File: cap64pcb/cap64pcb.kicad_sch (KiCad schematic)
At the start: 1 part

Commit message: first draft sch
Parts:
- added C1, C3: 10uF, Capacitor_SMD:C_0805_2012Metric, symbol Device:C_Small
- added C2: 1uF, Capacitor_SMD:C_0805_2012Metric, symbol Device:C_Small
- added C4, C5: 0.1uF, Capacitor_SMD:C_0805_2012Metric, symbol Device:C_Small
- added J1: SM05B_SURS_TF, Connector_JST:JST_SUR_SM05B-SURS-TF_1x05-1MP_P0.80mm_Horizontal, symbol Connector_Generic:Conn_01x05
- added JP1, JP2, JP3: SolderJumper_2_Open, Jumper:SolderJumper-2_P1.3mm_Open_RoundedPad1.0x1.5mm, symbol Jumper:SolderJumper_2_Open
- added JP4: SolderJumper_2_Bridged, Jumper:SolderJumper-2_P1.3mm_Bridged_RoundedPad1.0x1.5mm, symbol Jumper:SolderJumper_2_Bridged
- added Q1, Q2: BSS138, Package_TO_SOT_SMD:SOT-23, symbol Transistor_FET:BSS138
- added R1: 75kΩ, Resistor_SMD:R_0805_2012Metric, symbol Device:R_Small
- added TP1, TP10, TP11, TP12, TP2, TP3, TP4, TP5, TP6, TP7, TP8, TP9: TestPoint_Alt, symbol Connector:TestPoint_Alt
- added U2: SPX3819M5-L-3-3, Package_TO_SOT_SMD:SOT-23-5, symbol Regulator_Linear:SPX3819M5-L-3-3
- gave numbers to parts that had none: 1
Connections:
- net INT: now reaches U1.1 (~{IRQ})
- net INT: now also J1.4 (Pin_4)
- net at U1.10 (ELE2): now also TP3.1
- net at U1.11 (ELE3): now also TP4.1
- net at U1.12 (LED0/ELE4): now also TP5.1
- net at U1.13 (LED1/ELE5): now also TP6.1
- net at U1.14 (LED2/ELE6): now also TP7.1
- net at U1.15 (LED3/ELE7): now also TP8.1
- net at U1.16 (LED4/ELE8): now also TP9.1
- net at U1.17 (LED5/ELE9): now also TP10.1
- net at U1.18 (LED6/ELE10): now also TP11.1
- net at U1.19 (LED7/ELE11): now also TP12.1
- net SCL: now reaches U1.2 (SCL)
- net SCL: now also JP3.1 (A), Q2.2 (S)
- net +3V3: now reaches U1.20 (VDD)
- net +3V3: now also C3.1, C4.1, JP1.1 (A), Q1.1 (G), Q2.1 (G), U2.5 (OUT)
- net SDA: now reaches U1.3 (SDA)
- net SDA: now also JP2.1 (A), Q1.2 (S)
- net at U1.4 (ADDR): now also JP1.2 (B), JP2.2 (B), JP3.2 (B), JP4.2 (B)
- net at U1.5 (VREG): now also C5.1
- net GND: now reaches U1.6 (VSS)
- net GND: now also C1.2, C2.2, C3.2, C4.2, C5.2, J1.5 (Pin_5), JP4.1 (A), R1.2, U2.2 (GND)
- net at U1.7 (REXT): now also R1.1
- net at U1.8 (ELE0): now also TP1.1
- net at U1.9 (ELE1): now also TP2.1
- new net: C2.1, U2.4 (BP)
- new net: J1.2 (Pin_2), Q1.3 (D)
- new net: J1.3 (Pin_3), Q2.3 (D)
- new net VCC: C1.1, J1.1 (Pin_1), U2.1 (IN), U2.3 (EN)
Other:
- company: (none) -> beadybiddle
- title: (none) -> cap64
- moved on the sheet: U1

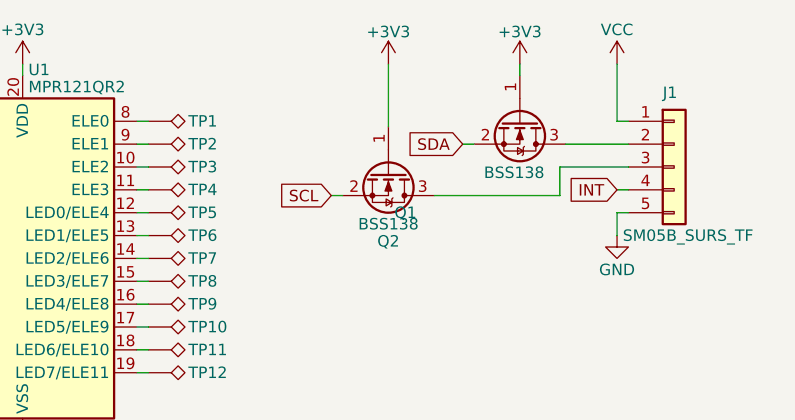
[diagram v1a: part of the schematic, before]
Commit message: pullup i2c 3v3 side lines
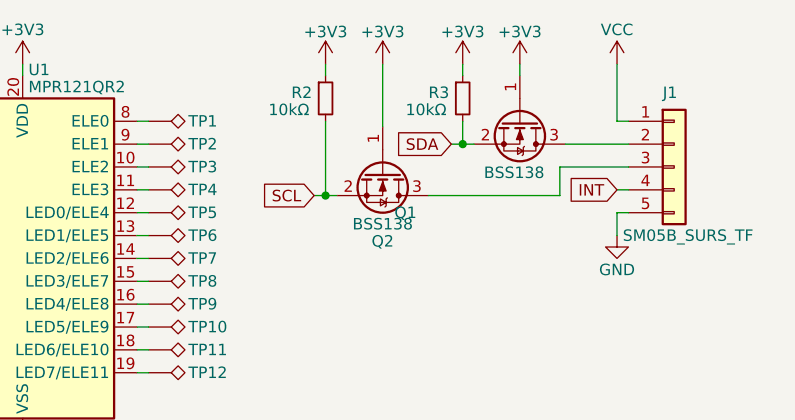
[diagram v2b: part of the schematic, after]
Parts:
- added R2, R3: 10kΩ, Resistor_SMD:R_0805_2012Metric, symbol Device:R_Small
- JP1: value SolderJumper_2_Open -> 3V3
- JP2: value SolderJumper_2_Open -> SDA
- JP3: value SolderJumper_2_Open -> SCL
- JP4: value SolderJumper_2_Bridged -> GND
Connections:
- net +3V3: now also R2.1, R3.1
- net SCL: now also R2.2
- net SDA: now also R3.2
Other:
- moved on the sheet: Q2

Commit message: cap pads
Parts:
- TP1: footprint (none) -> cap_pads:CAPPAD_8x8_Chevron_1
- TP10, TP11, TP2, TP3, TP4, TP5, TP6, TP7, TP8, TP9: footprint (none) -> cap_pads:CAPPAD_8x8_Chevron_2
- TP12: footprint (none) -> cap_pads:CAPPAD_8x8_Chevron_3
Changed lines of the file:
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@@
       (effects (font (size 1.27 1.27)) (justify left) hide)
     )
-    (property "Footprint" "" (id 2) (at 127 79.375 0)
+    (property "Footprint" "cap_pads:CAPPAD_8x8_Chevron_3" (id 2) (at 127 79.375 0)
       (effects (font (size 1.27 1.27)) hide)
     )
@@
       (effects (font (size 1.27 1.27)) (justify left) hide)
     )
-    (property "Footprint" "" (id 2) (at 127 71.755 0)
+    (property "Footprint" "cap_pads:CAPPAD_8x8_Chevron_2" (id 2) (at 127 71.755 0)
       (effects (font (size 1.27 1.27)) hide)
     )
@@
       (effects (font (size 1.27 1.27)) (justify left) hide)
     )
-    (property "Footprint" "" (id 2) (at 127 69.215 0)
+    (property "Footprint" "cap_pads:CAPPAD_8x8_Chevron_2" (id 2) (at 127 69.215 0)
       (effects (font (size 1.27 1.27)) hide)
     )
@@
       (effects (font (size 1.27 1.27)) (justify left) hide)
     )
-    (property "Footprint" "" (id 2) (at 127 76.835 0)
+    (property "Footprint" "cap_pads:CAPPAD_8x8_Chevron_2" (id 2) (at 127 76.835 0)
       (effects (font (size 1.27 1.27)) hide)
     )
@@
       (effects (font (size 1.27 1.27)) (justify left) hide)
     )
-    (property "Footprint" "" (id 2) (at 127 56.515 0)
+    (property "Footprint" "cap_pads:CAPPAD_8x8_Chevron_2" (id 2) (at 127 56.515 0)
       (effects (font (size 1.27 1.27)) hide)
     )
@@
       (effects (font (size 1.27 1.27)) (justify left) hide)
     )
-    (property "Footprint" "" (id 2) (at 127 61.595 0)
+    (property "Footprint" "cap_pads:CAPPAD_8x8_Chevron_2" (id 2) (at 127 61.595 0)
       (effects (font (size 1.27 1.27)) hide)
     )
@@
       (effects (font (size 1.27 1.27)) (justify left) hide)
     )
-    (property "Footprint" "" (id 2) (at 127 53.975 0)
+    (property "Footprint" "cap_pads:CAPPAD_8x8_Chevron_2" (id 2) (at 127 53.975 0)
       (effects (font (size 1.27 1.27)) hide)
     )
@@
       (effects (font (size 1.27 1.27)) (justify left) hide)
     )
-    (property "Footprint" "" (id 2) (at 127 66.675 0)
+    (property "Footprint" "cap_pads:CAPPAD_8x8_Chevron_2" (id 2) (at 127 66.675 0)
       (effects (font (size 1.27 1.27)) hide)
     )
@@
       (effects (font (size 1.27 1.27)) (justify left) hide)
     )
-    (property "Footprint" "" (id 2) (at 127 59.055 0)
+    (property "Footprint" "cap_pads:CAPPAD_8x8_Chevron_2" (id 2) (at 127 59.055 0)
       (effects (font (size 1.27 1.27)) hide)
     )
@@
       (effects (font (size 1.27 1.27)) (justify left) hide)
     )
-    (property "Footprint" "" (id 2) (at 127 51.435 0)
+    (property "Footprint" "cap_pads:CAPPAD_8x8_Chevron_1" (id 2) (at 127 51.435 0)
       (effects (font (size 1.27 1.27)) hide)
     )
@@
       (effects (font (size 1.27 1.27)) (justify left) hide)
     )
-    (property "Footprint" "" (id 2) (at 127 64.135 0)
+    (property "Footprint" "cap_pads:CAPPAD_8x8_Chevron_2" (id 2) (at 127 64.135 0)
       (effects (font (size 1.27 1.27)) hide)
     )
@@
       (effects (font (size 1.27 1.27)) (justify left) hide)
     )
-    (property "Footprint" "" (id 2) (at 127 74.295 0)
+    (property "Footprint" "cap_pads:CAPPAD_8x8_Chevron_2" (id 2) (at 127 74.295 0)
       (effects (font (size 1.27 1.27)) hide)
     )
@@
     )
     (path "/ba1958a1-7d76-4e1e-8b73-7c7712e56926"
-      (reference "TP1") (unit 1) (value "TestPoint_Alt") (footprint "")
+      (reference "TP1") (unit 1) (value "TestPoint_Alt") (footprint "cap_pads:CAPPAD_8x8_Chevron_1")
     )
     (path "/8b9944d7-de45-4c10-8f23-654b52f4b910"
-      (reference "TP2") (unit 1) (value "TestPoint_Alt") (footprint "")
+      (reference "TP2") (unit 1) (value "TestPoint_Alt") (footprint "cap_pads:CAPPAD_8x8_Chevron_2")
     )
     (path "/619d42dc-7a77-4d03-bcdd-97078c405047"
-      (reference "TP3") (unit 1) (value "TestPoint_Alt") (footprint "")
+      (reference "TP3") (unit 1) (value "TestPoint_Alt") (footprint "cap_pads:CAPPAD_8x8_Chevron_2")
     )
     (path "/b829908f-cd58-4d41-823c-96c17337397b"
-      (reference "TP4") (unit 1) (value "TestPoint_Alt") (footprint "")
+      (reference "TP4") (unit 1) (value "TestPoint_Alt") (footprint "cap_pads:CAPPAD_8x8_Chevron_2")
     )
     (path "/625a82e9-f251-4d4b-85a0-987cbbd608cd"
-      (reference "TP5") (unit 1) (value "TestPoint_Alt") (footprint "")
+      (reference "TP5") (unit 1) (value "TestPoint_Alt") (footprint "cap_pads:CAPPAD_8x8_Chevron_2")
     )
     (path "/bc614aae-bf8a-4524-b8fb-f2986c6a385f"
-      (reference "TP6") (unit 1) (value "TestPoint_Alt") (footprint "")
+      (reference "TP6") (unit 1) (value "TestPoint_Alt") (footprint "cap_pads:CAPPAD_8x8_Chevron_2")
     )
     (path "/b13c650d-d345-428a-ba03-fd5871ca5c98"
-      (reference "TP7") (unit 1) (value "TestPoint_Alt") (footprint "")
+      (reference "TP7") (unit 1) (value "TestPoint_Alt") (footprint "cap_pads:CAPPAD_8x8_Chevron_2")
     )
     (path "/4e184203-7c1c-4b52-a73a-be217f4bb796"
-      (reference "TP8") (unit 1) (value "TestPoint_Alt") (footprint "")
+      (reference "TP8") (unit 1) (value "TestPoint_Alt") (footprint "cap_pads:CAPPAD_8x8_Chevron_2")
     )
     (path "/39942e6b-3cc0-4ee7-8c07-44ca728f58d6"
-      (reference "TP9") (unit 1) (value "TestPoint_Alt") (footprint "")
+      (reference "TP9") (unit 1) (value "TestPoint_Alt") (footprint "cap_pads:CAPPAD_8x8_Chevron_2")
     )
     (path "/f030bf22-0011-4c17-a015-6e34a85a327f"
-      (reference "TP10") (unit 1) (value "TestPoint_Alt") (footprint "")
+      (reference "TP10") (unit 1) (value "TestPoint_Alt") (footprint "cap_pads:CAPPAD_8x8_Chevron_2")
     )
     (path "/5200f4f7-8155-455b-8d82-55039fa33a17"
-      (reference "TP11") (unit 1) (value "TestPoint_Alt") (footprint "")
+      (reference "TP11") (unit 1) (value "TestPoint_Alt") (footprint "cap_pads:CAPPAD_8x8_Chevron_2")
     )
     (path "/1db37ab1-6540-4715-a5f1-8f515d3788c5"
-      (reference "TP12") (unit 1) (value "TestPoint_Alt") (footprint "")
+      (reference "TP12") (unit 1) (value "TestPoint_Alt") (footprint "cap_pads:CAPPAD_8x8_Chevron_3")
     )
     (path "/c8c3ab22-4b33-4bf7-93a7-fa49e1af3364"

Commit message: fixed miniscule spacing error
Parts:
- TP1: footprint cap_pads:CAPPAD_8x8_Chevron_1 -> cap_pads:CAPPAD_7.6x7.6_Chevron_1
- TP10, TP11, TP2, TP3, TP4, TP5, TP6, TP7, TP8, TP9: footprint cap_pads:CAPPAD_8x8_Chevron_2 -> cap_pads:CAPPAD_7.6x7.6_Chevron_2
- TP12: footprint cap_pads:CAPPAD_8x8_Chevron_3 -> cap_pads:CAPPAD_7.6x7.6_Chevron_3
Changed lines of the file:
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@@
       (effects (font (size 1.27 1.27)) (justify left) hide)
     )
-    (property "Footprint" "cap_pads:CAPPAD_8x8_Chevron_3" (id 2) (at 127 79.375 0)
+    (property "Footprint" "cap_pads:CAPPAD_7.6x7.6_Chevron_3" (id 2) (at 127 79.375 0)
       (effects (font (size 1.27 1.27)) hide)
     )
@@
       (effects (font (size 1.27 1.27)) (justify left) hide)
     )
-    (property "Footprint" "cap_pads:CAPPAD_8x8_Chevron_2" (id 2) (at 127 71.755 0)
+    (property "Footprint" "cap_pads:CAPPAD_7.6x7.6_Chevron_2" (id 2) (at 127 71.755 0)
       (effects (font (size 1.27 1.27)) hide)
     )
@@
       (effects (font (size 1.27 1.27)) (justify left) hide)
     )
-    (property "Footprint" "cap_pads:CAPPAD_8x8_Chevron_2" (id 2) (at 127 69.215 0)
+    (property "Footprint" "cap_pads:CAPPAD_7.6x7.6_Chevron_2" (id 2) (at 127 69.215 0)
       (effects (font (size 1.27 1.27)) hide)
     )
@@
       (effects (font (size 1.27 1.27)) (justify left) hide)
     )
-    (property "Footprint" "cap_pads:CAPPAD_8x8_Chevron_2" (id 2) (at 127 76.835 0)
+    (property "Footprint" "cap_pads:CAPPAD_7.6x7.6_Chevron_2" (id 2) (at 127 76.835 0)
       (effects (font (size 1.27 1.27)) hide)
     )
@@
       (effects (font (size 1.27 1.27)) (justify left) hide)
     )
-    (property "Footprint" "cap_pads:CAPPAD_8x8_Chevron_2" (id 2) (at 127 56.515 0)
+    (property "Footprint" "cap_pads:CAPPAD_7.6x7.6_Chevron_2" (id 2) (at 127 56.515 0)
       (effects (font (size 1.27 1.27)) hide)
     )
@@
       (effects (font (size 1.27 1.27)) (justify left) hide)
     )
-    (property "Footprint" "cap_pads:CAPPAD_8x8_Chevron_2" (id 2) (at 127 61.595 0)
+    (property "Footprint" "cap_pads:CAPPAD_7.6x7.6_Chevron_2" (id 2) (at 127 61.595 0)
       (effects (font (size 1.27 1.27)) hide)
     )
@@
       (effects (font (size 1.27 1.27)) (justify left) hide)
     )
-    (property "Footprint" "cap_pads:CAPPAD_8x8_Chevron_2" (id 2) (at 127 53.975 0)
+    (property "Footprint" "cap_pads:CAPPAD_7.6x7.6_Chevron_2" (id 2) (at 127 53.975 0)
       (effects (font (size 1.27 1.27)) hide)
     )
@@
       (effects (font (size 1.27 1.27)) (justify left) hide)
     )
-    (property "Footprint" "cap_pads:CAPPAD_8x8_Chevron_2" (id 2) (at 127 66.675 0)
+    (property "Footprint" "cap_pads:CAPPAD_7.6x7.6_Chevron_2" (id 2) (at 127 66.675 0)
       (effects (font (size 1.27 1.27)) hide)
     )
@@
       (effects (font (size 1.27 1.27)) (justify left) hide)
     )
-    (property "Footprint" "cap_pads:CAPPAD_8x8_Chevron_2" (id 2) (at 127 59.055 0)
+    (property "Footprint" "cap_pads:CAPPAD_7.6x7.6_Chevron_2" (id 2) (at 127 59.055 0)
       (effects (font (size 1.27 1.27)) hide)
     )
@@
       (effects (font (size 1.27 1.27)) (justify left) hide)
     )
-    (property "Footprint" "cap_pads:CAPPAD_8x8_Chevron_1" (id 2) (at 127 51.435 0)
+    (property "Footprint" "cap_pads:CAPPAD_7.6x7.6_Chevron_1" (id 2) (at 127 51.435 0)
       (effects (font (size 1.27 1.27)) hide)
     )
@@
       (effects (font (size 1.27 1.27)) (justify left) hide)
     )
-    (property "Footprint" "cap_pads:CAPPAD_8x8_Chevron_2" (id 2) (at 127 64.135 0)
+    (property "Footprint" "cap_pads:CAPPAD_7.6x7.6_Chevron_2" (id 2) (at 127 64.135 0)
       (effects (font (size 1.27 1.27)) hide)
     )
@@
       (effects (font (size 1.27 1.27)) (justify left) hide)
     )
-    (property "Footprint" "cap_pads:CAPPAD_8x8_Chevron_2" (id 2) (at 127 74.295 0)
+    (property "Footprint" "cap_pads:CAPPAD_7.6x7.6_Chevron_2" (id 2) (at 127 74.295 0)
       (effects (font (size 1.27 1.27)) hide)
     )
@@
     )
     (path "/ba1958a1-7d76-4e1e-8b73-7c7712e56926"
-      (reference "TP1") (unit 1) (value "TestPoint_Alt") (footprint "cap_pads:CAPPAD_8x8_Chevron_1")
+      (reference "TP1") (unit 1) (value "TestPoint_Alt") (footprint "cap_pads:CAPPAD_7.6x7.6_Chevron_1")
     )
     (path "/8b9944d7-de45-4c10-8f23-654b52f4b910"
-      (reference "TP2") (unit 1) (value "TestPoint_Alt") (footprint "cap_pads:CAPPAD_8x8_Chevron_2")
+      (reference "TP2") (unit 1) (value "TestPoint_Alt") (footprint "cap_pads:CAPPAD_7.6x7.6_Chevron_2")
     )
     (path "/619d42dc-7a77-4d03-bcdd-97078c405047"
-      (reference "TP3") (unit 1) (value "TestPoint_Alt") (footprint "cap_pads:CAPPAD_8x8_Chevron_2")
+      (reference "TP3") (unit 1) (value "TestPoint_Alt") (footprint "cap_pads:CAPPAD_7.6x7.6_Chevron_2")
     )
     (path "/b829908f-cd58-4d41-823c-96c17337397b"
-      (reference "TP4") (unit 1) (value "TestPoint_Alt") (footprint "cap_pads:CAPPAD_8x8_Chevron_2")
+      (reference "TP4") (unit 1) (value "TestPoint_Alt") (footprint "cap_pads:CAPPAD_7.6x7.6_Chevron_2")
     )
     (path "/625a82e9-f251-4d4b-85a0-987cbbd608cd"
-      (reference "TP5") (unit 1) (value "TestPoint_Alt") (footprint "cap_pads:CAPPAD_8x8_Chevron_2")
+      (reference "TP5") (unit 1) (value "TestPoint_Alt") (footprint "cap_pads:CAPPAD_7.6x7.6_Chevron_2")
     )
     (path "/bc614aae-bf8a-4524-b8fb-f2986c6a385f"
-      (reference "TP6") (unit 1) (value "TestPoint_Alt") (footprint "cap_pads:CAPPAD_8x8_Chevron_2")
+      (reference "TP6") (unit 1) (value "TestPoint_Alt") (footprint "cap_pads:CAPPAD_7.6x7.6_Chevron_2")
     )
     (path "/b13c650d-d345-428a-ba03-fd5871ca5c98"
-      (reference "TP7") (unit 1) (value "TestPoint_Alt") (footprint "cap_pads:CAPPAD_8x8_Chevron_2")
+      (reference "TP7") (unit 1) (value "TestPoint_Alt") (footprint "cap_pads:CAPPAD_7.6x7.6_Chevron_2")
     )
     (path "/4e184203-7c1c-4b52-a73a-be217f4bb796"
-      (reference "TP8") (unit 1) (value "TestPoint_Alt") (footprint "cap_pads:CAPPAD_8x8_Chevron_2")
+      (reference "TP8") (unit 1) (value "TestPoint_Alt") (footprint "cap_pads:CAPPAD_7.6x7.6_Chevron_2")
     )
     (path "/39942e6b-3cc0-4ee7-8c07-44ca728f58d6"
-      (reference "TP9") (unit 1) (value "TestPoint_Alt") (footprint "cap_pads:CAPPAD_8x8_Chevron_2")
+      (reference "TP9") (unit 1) (value "TestPoint_Alt") (footprint "cap_pads:CAPPAD_7.6x7.6_Chevron_2")
     )
     (path "/f030bf22-0011-4c17-a015-6e34a85a327f"
-      (reference "TP10") (unit 1) (value "TestPoint_Alt") (footprint "cap_pads:CAPPAD_8x8_Chevron_2")
+      (reference "TP10") (unit 1) (value "TestPoint_Alt") (footprint "cap_pads:CAPPAD_7.6x7.6_Chevron_2")
     )
     (path "/5200f4f7-8155-455b-8d82-55039fa33a17"
-      (reference "TP11") (unit 1) (value "TestPoint_Alt") (footprint "cap_pads:CAPPAD_8x8_Chevron_2")
+      (reference "TP11") (unit 1) (value "TestPoint_Alt") (footprint "cap_pads:CAPPAD_7.6x7.6_Chevron_2")
     )
     (path "/1db37ab1-6540-4715-a5f1-8f515d3788c5"
-      (reference "TP12") (unit 1) (value "TestPoint_Alt") (footprint "cap_pads:CAPPAD_8x8_Chevron_3")
+      (reference "TP12") (unit 1) (value "TestPoint_Alt") (footprint "cap_pads:CAPPAD_7.6x7.6_Chevron_3")
     )
     (path "/c8c3ab22-4b33-4bf7-93a7-fa49e1af3364"

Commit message: rough 1-6 routing
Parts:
- TP6, TP7: footprint cap_pads:CAPPAD_7.6x7.6_Chevron_2 -> cap_pads:CAPPAD_7.6x7.6_Chevron_2_shifted
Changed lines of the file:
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@@
       (effects (font (size 1.27 1.27)) (justify left) hide)
     )
-    (property "Footprint" "cap_pads:CAPPAD_7.6x7.6_Chevron_2" (id 2) (at 127 66.675 0)
+    (property "Footprint" "cap_pads:CAPPAD_7.6x7.6_Chevron_2_shifted" (id 2) (at 127 66.675 0)
       (effects (font (size 1.27 1.27)) hide)
     )
@@
       (effects (font (size 1.27 1.27)) (justify left) hide)
     )
-    (property "Footprint" "cap_pads:CAPPAD_7.6x7.6_Chevron_2" (id 2) (at 127 64.135 0)
+    (property "Footprint" "cap_pads:CAPPAD_7.6x7.6_Chevron_2_shifted" (id 2) (at 127 64.135 0)
       (effects (font (size 1.27 1.27)) hide)
     )
@@
     )
     (path "/bc614aae-bf8a-4524-b8fb-f2986c6a385f"
-      (reference "TP6") (unit 1) (value "TestPoint_Alt") (footprint "cap_pads:CAPPAD_7.6x7.6_Chevron_2")
+      (reference "TP6") (unit 1) (value "TestPoint_Alt") (footprint "cap_pads:CAPPAD_7.6x7.6_Chevron_2_shifted")
     )
     (path "/b13c650d-d345-428a-ba03-fd5871ca5c98"
-      (reference "TP7") (unit 1) (value "TestPoint_Alt") (footprint "cap_pads:CAPPAD_7.6x7.6_Chevron_2")
+      (reference "TP7") (unit 1) (value "TestPoint_Alt") (footprint "cap_pads:CAPPAD_7.6x7.6_Chevron_2_shifted")
     )
     (path "/4e184203-7c1c-4b52-a73a-be217f4bb796"
